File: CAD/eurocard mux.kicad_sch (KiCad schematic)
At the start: 4 parts, among them J1 Conn_01x16, J2 Conn_01x16, J3 Conn_01x16, J4 Screw_Terminal_01x16

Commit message: new relays
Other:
- company: (none) -> NMBU-Mina
- title: (none) -> SPI-MUX

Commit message: Feat:Fixed digikey partnumbers, rexport, 3d mod
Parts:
- J1, J2, J3: Digikey (none) -> 3020-16-0200-00; LCSC Part # (none) -> 3020-16-0200-00
- J4: Digikey (none) -> TB003-500-P16BE; LCSC Part # (none) -> TB003-500-P16BE
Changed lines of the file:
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@@
+      (effects (font (size 1.27 1.27)) hide)
+    )
+    (property "Digikey" "3020-16-0200-00" (id 4) (at 19.05 146.05 0)
+      (effects (font (size 1.27 1.27)) hide)
+    )
+    (property "LCSC Part #" "3020-16-0200-00" (id 5) (at 19.05 146.05 0)
       (effects (font (size 1.27 1.27)) hide)
     )
@@
       (effects (font (size 1.27 1.27)) hide)
     )
+    (property "Digikey" "3020-16-0200-00" (id 4) (at 21.59 48.26 0)
+      (effects (font (size 1.27 1.27)) hide)
+    )
+    (property "LCSC Part #" "3020-16-0200-00" (id 5) (at 21.59 48.26 0)
+      (effects (font (size 1.27 1.27)) hide)
+    )
     (pin "1")
     (pin "10")
@@
       (effects (font (size 1.27 1.27)) hide)
     )
+    (property "Digikey" "3020-16-0200-00" (id 4) (at 200.66 81.28 0)
+      (effects (font (size 1.27 1.27)) hide)
+    )
+    (property "LCSC Part #" "3020-16-0200-00" (id 5) (at 200.66 81.28 0)
+      (effects (font (size 1.27 1.27)) hide)
+    )
     (pin "1")
     (pin "10")
@@
       (effects (font (size 1.27 1.27)) hide)
     )
+    (property "Digikey" "TB003-500-P16BE" (id 4) (at 247.65 83.82 0)
+      (effects (font (size 1.27 1.27)) hide)
+    )
+    (property "LCSC Part #" "TB003-500-P16BE" (id 5) (at 247.65 83.82 0)
+      (effects (font (size 1.27 1.27)) hide)
+    )

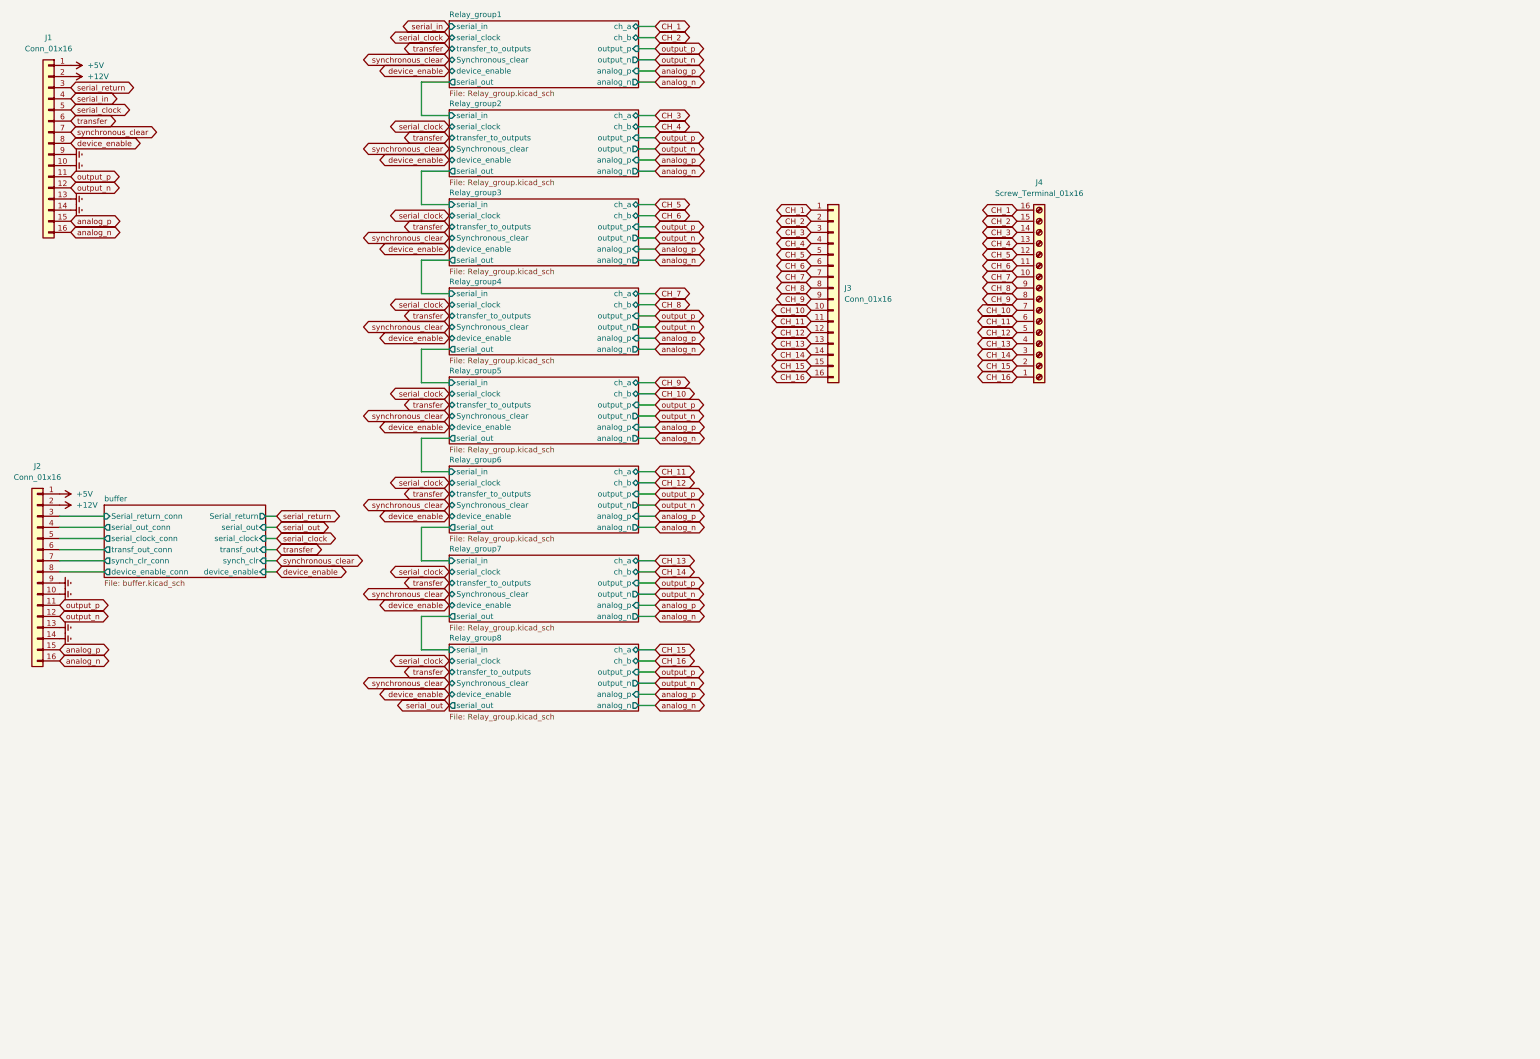
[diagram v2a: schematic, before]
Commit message: Feat: Single side test
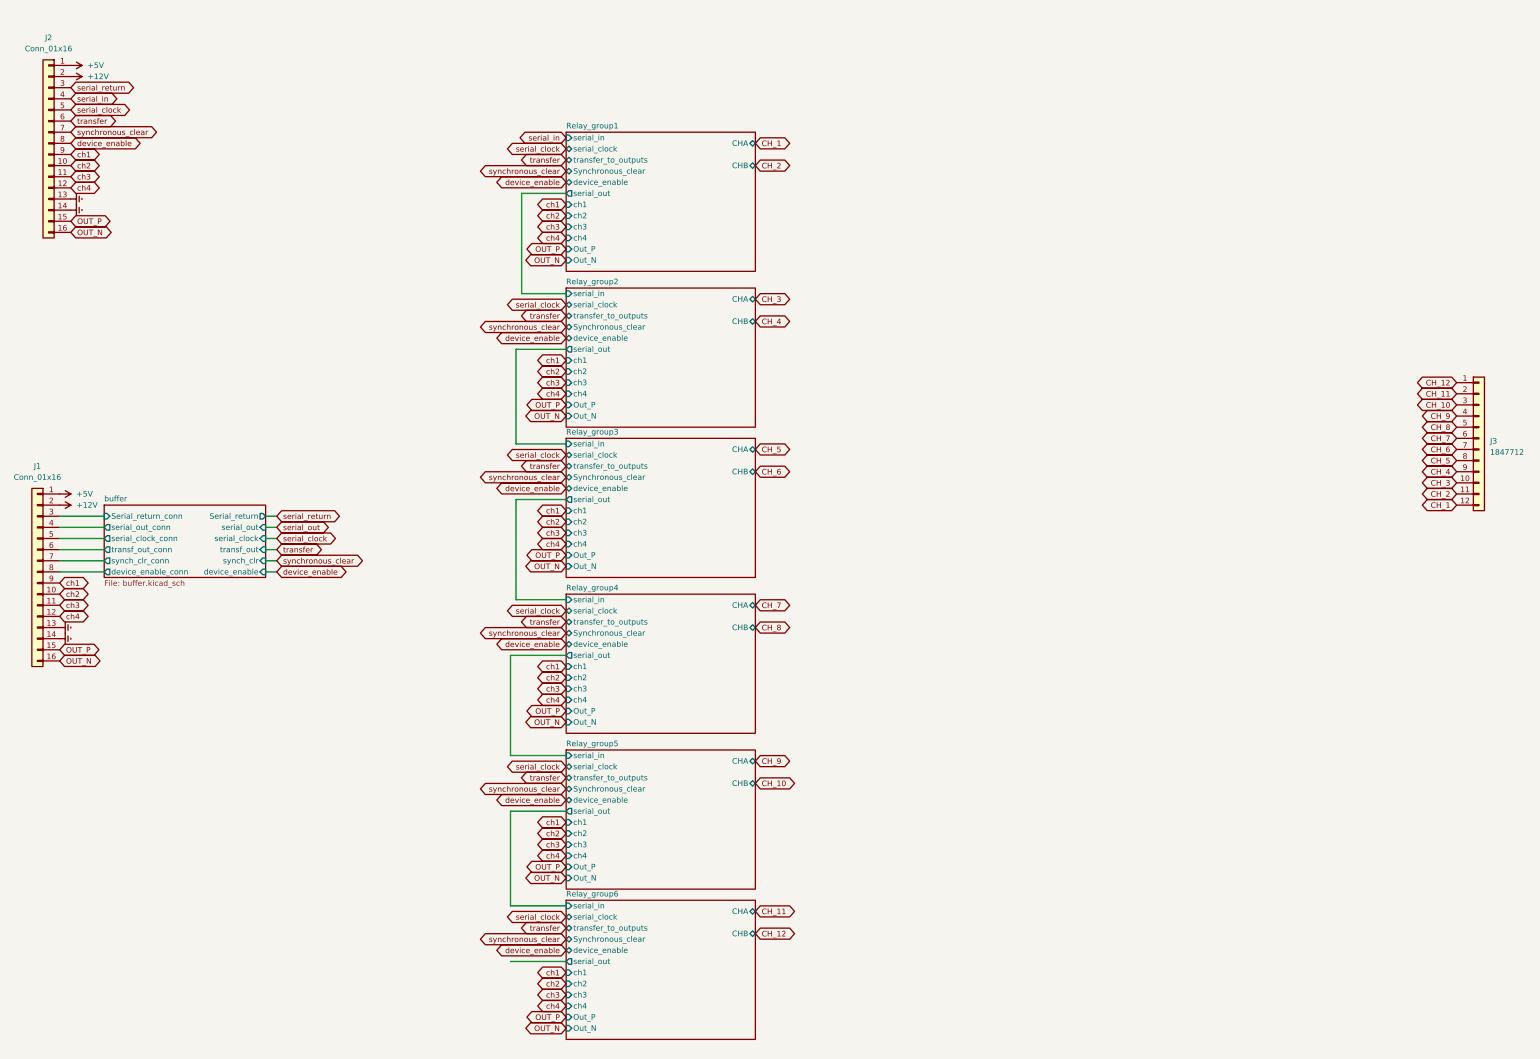
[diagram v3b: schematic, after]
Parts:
- removed J3: Conn_01x16, Connector_IDC:IDC-Header_2x08_P2.54mm_Vertical, symbol Connector_Generic:Conn_01x16
- removed J4: Screw_Terminal_01x16, TerminalBlock_Phoenix:TerminalBlock_Phoenix_MKDS-1,5-16_1x16_P5.00mm_Horizontal, symbol Connector:Screw_Terminal_01x16
- added J3: 1847712, Connector_Phoenix_MC_HighVoltage:PhoenixContact_MC_1,5_12-GF-5.08_1x12_P5.08mm_Horizontal_ThreadedFlange_MountHole, symbol Connector_Generic:Conn_01x12
- J1: renamed from J2; footprint Connector_IDC:IDC-Header_2x08_P2.54mm_Horizontal -> Connector_IDC:IDC-Header_2x08_P2.54mm_Vertical
- J2: renamed from J1; footprint Connector_IDC:IDC-Header_2x08_P2.54mm_Horizontal -> Connector_IDC:IDC-Header_2x08_P2.54mm_Vertical
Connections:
- net CH_1: now also J3.12 (Pin_12)
- net CH_10: now also J3.3 (Pin_3)
- net CH_11: now also J3.2 (Pin_2)
- net CH_12: now also J3.1 (Pin_1)
- net CH_2: now also J3.11 (Pin_11)
- net CH_3: now also J3.10 (Pin_10)
- net CH_4: now also J3.9 (Pin_9)
- net CH_5: now also J3.8 (Pin_8)
- net CH_6: now also J3.7 (Pin_7)
- net CH_7: now also J3.6 (Pin_6)
- net CH_8: now also J3.5 (Pin_5)
- net CH_9: now also J3.4 (Pin_4)
- net Earth: no longer J1.10 (Pin_10), J1.9 (Pin_9), J2.10 (Pin_10), J2.9 (Pin_9)
- net analog_n renamed OUT_N
- net analog_p renamed OUT_P
- net output_n renamed ch4
- net output_p renamed ch3
- new net ch1: J1.9 (Pin_9), J2.9 (Pin_9)
- new net ch2: J1.10 (Pin_10), J2.10 (Pin_10)
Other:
- removed sheet Relay_group7
- removed sheet Relay_group8
- sheet Relay_group1 ports: added CHA, CHB, Out_N, Out_P, ch1, ch2, ch3, ch4; removed analog_n, analog_p, ch_a, ch_b, output_n, output_p
- sheet Relay_group2 ports: added CHA, CHB, Out_N, Out_P, ch1, ch2, ch3, ch4; removed analog_n, analog_p, ch_a, ch_b, output_n, output_p
- sheet Relay_group3 ports: added CHA, CHB, Out_N, Out_P, ch1, ch2, ch3, ch4; removed analog_n, analog_p, ch_a, ch_b, output_n, output_p
- sheet Relay_group4 ports: added CHA, CHB, Out_N, Out_P, ch1, ch2, ch3, ch4; removed analog_n, analog_p, ch_a, ch_b, output_n, output_p
- sheet Relay_group5 ports: added CHA, CHB, Out_N, Out_P, ch1, ch2, ch3, ch4; removed analog_n, analog_p, ch_a, ch_b, output_n, output_p
- sheet Relay_group6 ports: added CHA, CHB, Out_N, Out_P, ch1, ch2, ch3, ch4; removed analog_n, analog_p, ch_a, ch_b, output_n, output_p

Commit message: Feat: WIP
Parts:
- added J4: 1847712, Connector_Phoenix_MC_HighVoltage:PhoenixContact_MC_1,5_12-GF-5.08_1x12_P5.08mm_Horizontal_ThreadedFlange_MountHole, symbol Connector_Generic:Conn_01x12
- J1, J2: footprint Connector_IDC:IDC-Header_2x08_P2.54mm_Vertical -> Connector_IDC:IDC-Header_2x08_P2.54mm_Horizontal
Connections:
- new net CH_13: J4.12 (Pin_12)
- new net CH_14: J4.11 (Pin_11)
- new net CH_15: J4.10 (Pin_10)
- new net CH_16: J4.9 (Pin_9)
- new net CH_17: J4.8 (Pin_8)
- new net CH_18: J4.7 (Pin_7)
- new net CH_19: J4.6 (Pin_6)
- new net CH_20: J4.5 (Pin_5)
- new net CH_21: J4.4 (Pin_4)
- new net CH_22: J4.3 (Pin_3)
- new net CH_23: J4.2 (Pin_2)
- new net CH_24: J4.1 (Pin_1)
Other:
- added sheet Relay_group10 (Relay_group.kicad_sch)
- added sheet Relay_group11 (Relay_group.kicad_sch)
- added sheet Relay_group12 (Relay_group.kicad_sch)
- added sheet Relay_group7 (Relay_group.kicad_sch)
- added sheet Relay_group8 (Relay_group.kicad_sch)
- added sheet Relay_group9 (Relay_group.kicad_sch)

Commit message: Feat:WIP push
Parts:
- added J5, J6: Conn_01x02, Connector_Phoenix_MC_HighVoltage:PhoenixContact_MC_1,5_2-G-5.08_1x02_P5.08mm_Horizontal, symbol Connector_Generic:Conn_01x02
- added JP1, JP2, JP3, JP4: Jumper_2_Bridged, Resistor_SMD:R_0805_2012Metric, symbol Jumper:Jumper_2_Bridged
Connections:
- net OUT_N: now also J5.1 (Pin_1), J6.1 (Pin_1), JP2.2 (B), JP4.2 (B); no longer J1.16 (Pin_16), J2.16 (Pin_16)
- net OUT_P: now also J5.2 (Pin_2), J6.2 (Pin_2), JP1.2 (B), JP3.2 (B); no longer J1.15 (Pin_15), J2.15 (Pin_15)
- new net: J1.15 (Pin_15), JP3.1 (A)
- new net: J1.16 (Pin_16), JP4.1 (A)
- new net: J2.15 (Pin_15), JP1.1 (A)
- new net: J2.16 (Pin_16), JP2.1 (A)
